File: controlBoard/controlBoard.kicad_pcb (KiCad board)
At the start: 2 copper layers, 37.5 x 35 mm, 32 parts, among them J1 FTDI, J2 Servo, J3 Fingerprint, J4 Barrel_Jack_Switch, J5 ICSP, SW1 SW_Push, SW2 SW_Push, SW3 SW_Push, U1 ATmega328P-AU, U2 PCA9685BS, U3 AP2112K-3.3TRG1, Y1 Crystal

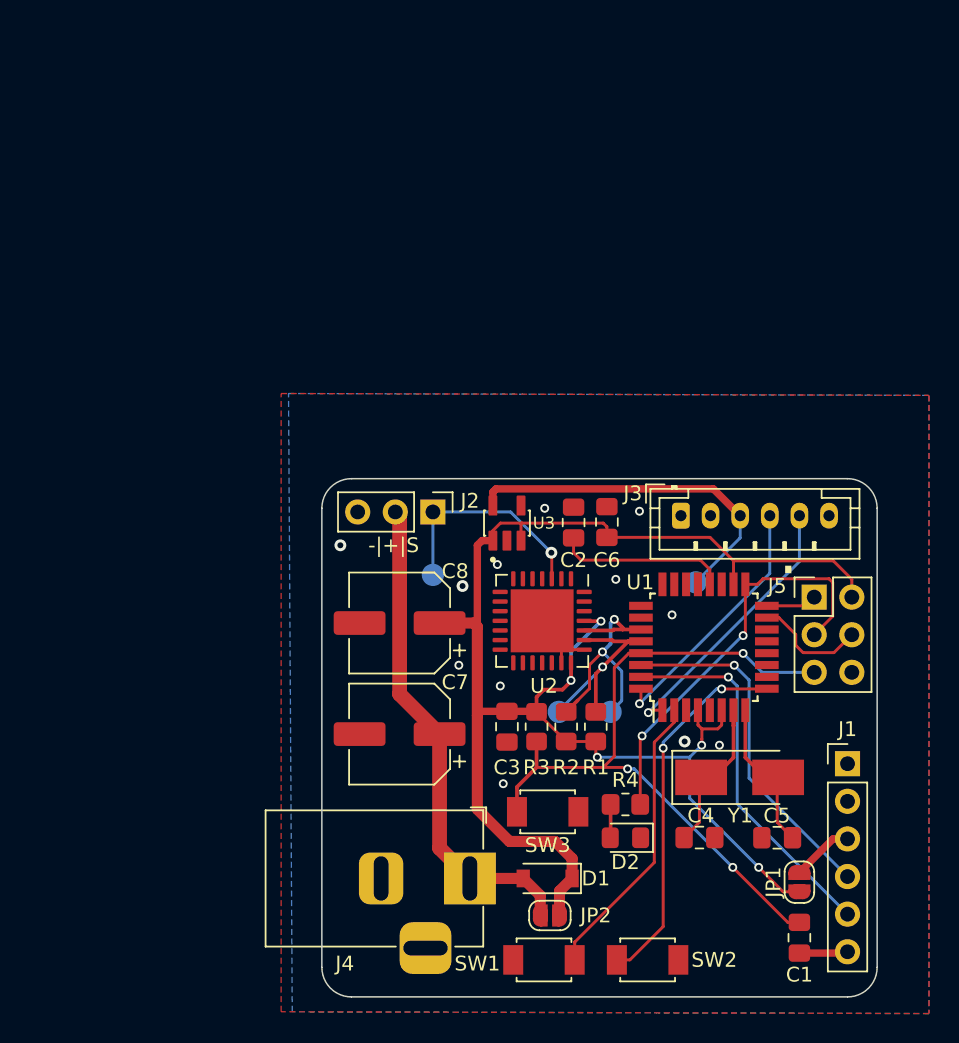
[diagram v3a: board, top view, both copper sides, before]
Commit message: Added decoupling cap for fingerprint reader, generated gerbers
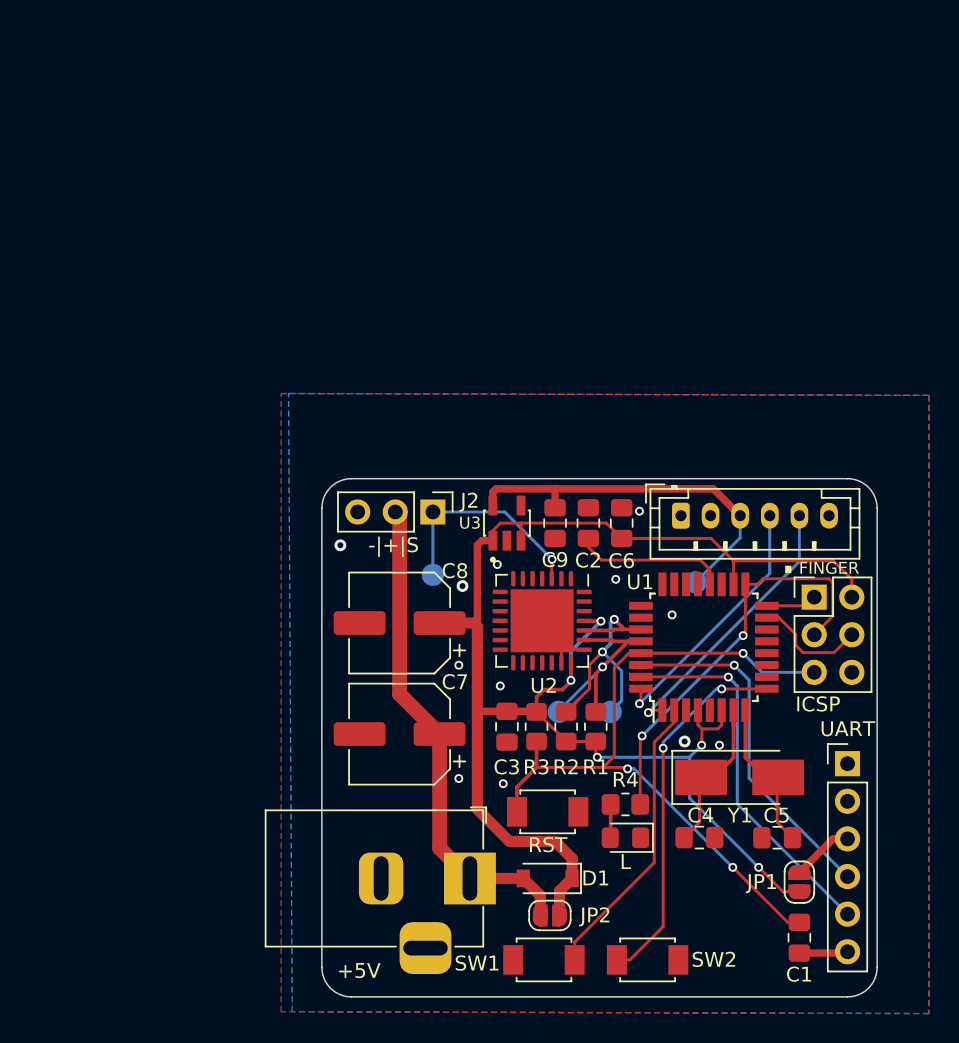
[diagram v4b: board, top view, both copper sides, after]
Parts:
- added C9: 100n, Capacitor_SMD:C_0805_2012Metric_Pad1.18x1.45mm_HandSolder, F.Cu at (156.5, 69.0)
- moved C6 1.00 mm to (161.0, 69.0)
- moved C2 1.00 mm to (158.8, 69.0)
- renumbered J4 to +5V, J3 to FINGER, J5 to ICSP, D2 to L, SW3 to RST, J1 to UART
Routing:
- net +3V3: track 24.2 -> 25.5 mm
- net Net-(C2-Pad1): track 11.7 -> 10.4 mm
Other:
- board text added: "+5Vin"
- board text added: "+5V|MISO MOSI|SCK - |RST"
- board text added: "Fingerprint Doorlock v1.1 UIUC 2021"
- board text removed: "+ |MISO MOSI|SCK - | RST"
- board text removed: "Fingerprint Doorlock v1.0 UIUC 2021"
- board text removed: "VCC"
